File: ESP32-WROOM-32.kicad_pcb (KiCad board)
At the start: 2 copper layers, 80 x 80 mm, 26 parts, among them J1 Conn_01x10_Pin, J2 USB_C_Receptacle_USB2.0_16P, J3 Conn_01x10_Pin, J5 Conn_01x05, Q1 S8050, Q2 S8050, SW1 SW_Push, SW2 SW_Push, U1 ESP32-WROOM-32E, U2 AMS1117-3.3, U3 CH340C

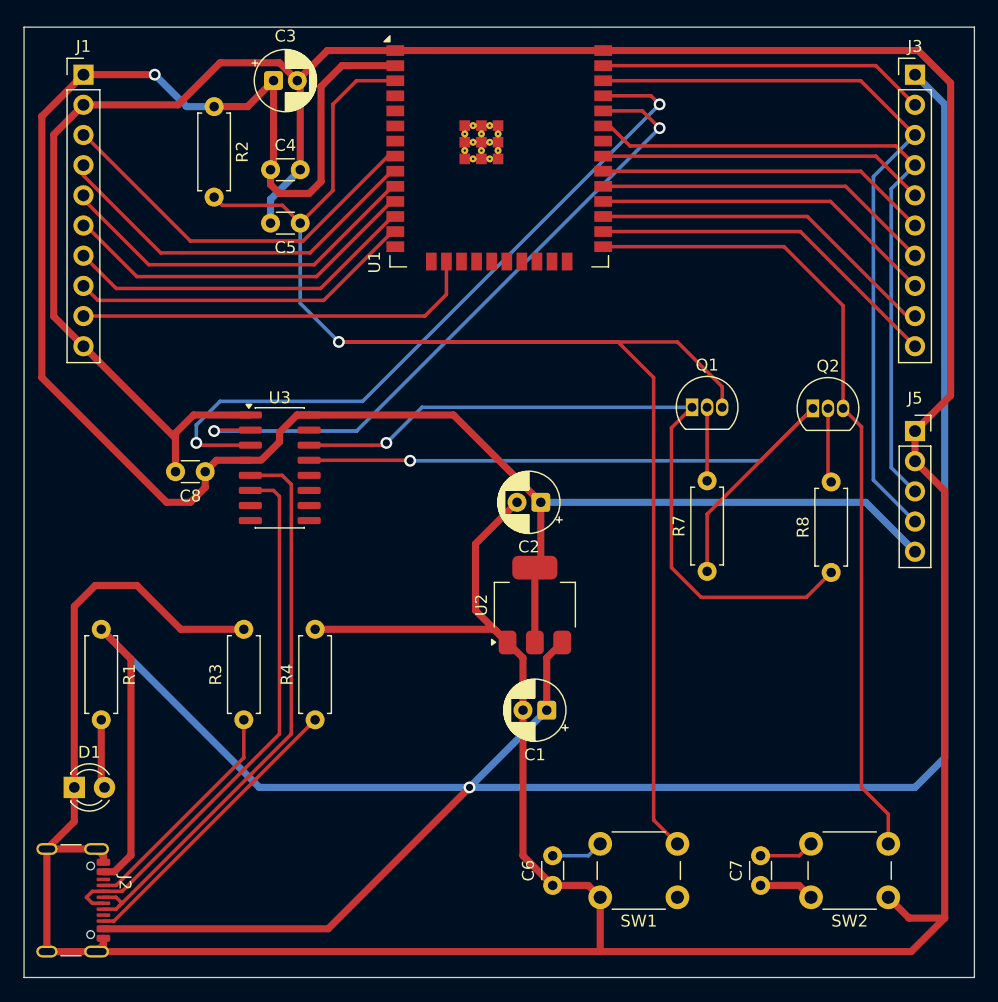
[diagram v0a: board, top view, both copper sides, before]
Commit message: Clean up KiCad project files
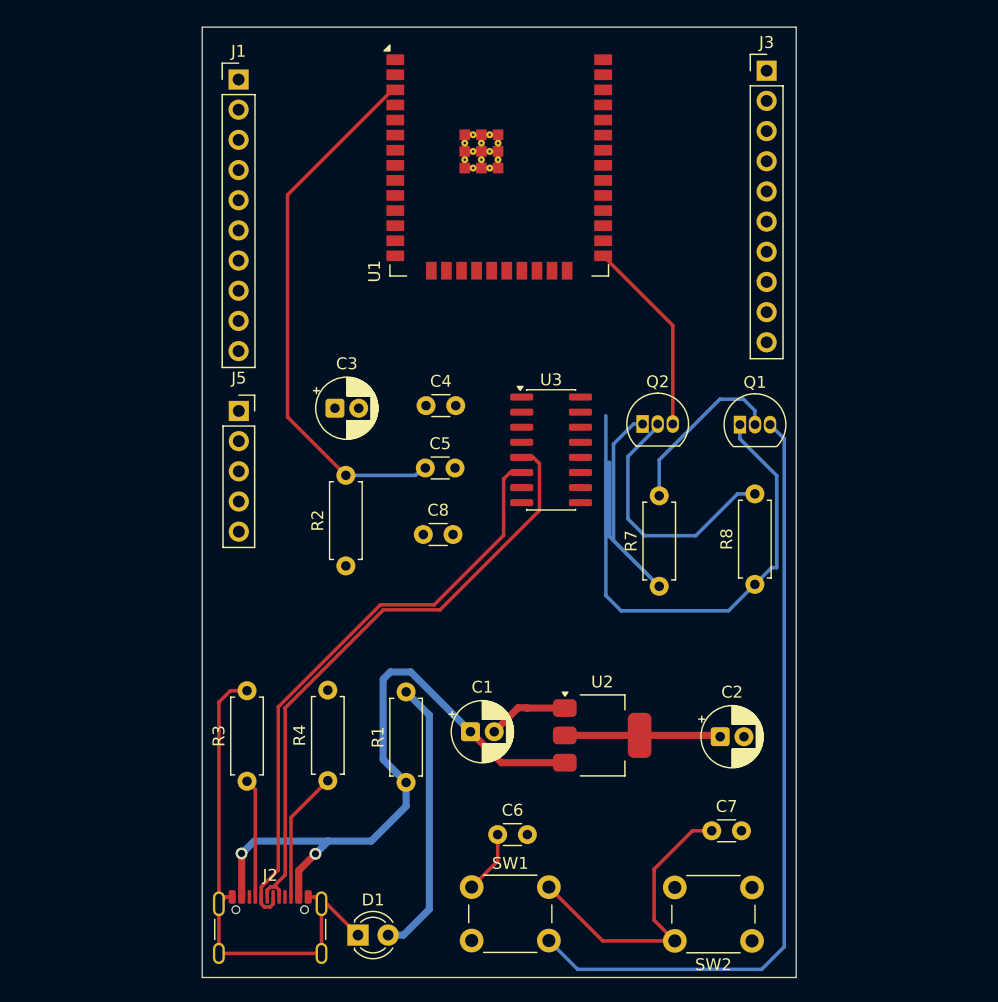
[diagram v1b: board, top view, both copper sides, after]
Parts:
- moved J5 56.9 mm to (128.1, 92.3)
- moved R2 40.2 mm to (137.1, 105.3), turned to 90 degrees
- moved R1 28.7 mm to (142.2, 123.6), turned to 90 degrees
- moved C3 28.1 mm to (136.2, 92.1)
- moved D1 26.9 mm to (138.1, 136.4)
- moved C2 24.8 mm to (168.6, 119.7), turned to 0 degrees
- moved C4 23.8 mm to (143.8, 91.9)
- moved C5 23.1 mm to (143.8, 97.1), turned to 0 degrees
- moved U3 22.9 mm to (154.4, 95.6)
- moved C8 19.1 mm to (143.6, 102.7), turned to 0 degrees
- moved J2 18.0 mm to (130.7, 136.9), turned to 0 degrees
- moved SW1 17.3 mm to (147.7, 132.4), turned to 0 degrees
- moved Q2 14.4 mm to (162.1, 93.4)
- moved J1 13.1 mm to (128.1, 64.4)
- moved J3 12.5 mm to (172.5, 63.7)
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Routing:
- net GND: track 411.6 -> 81.1 mm
- net +3V3: track 171.7 -> 13.1 mm, vias 1 -> 0
- net +5V: track 210.2 -> 55.1 mm, vias 1 -> 2
- net /IO22: track 63.6 -> 0.00 mm
- net /TXD0: track 61.4 -> 0.00 mm, vias 2 -> 0
- net /IO0: track 73.8 -> 16.6 mm
- net /IO21: track 56.7 -> 0.00 mm
- net /RXD0: track 56.5 -> 0.00 mm, vias 2 -> 0
- net /IO13: track 34.1 -> 0.00 mm
- net /EN: track 144.5 -> 111.4 mm, vias 1 -> 0
- net /IO32: track 32.9 -> 0.00 mm
- net /DTR: track 61.6 -> 28.9 mm, vias 1 -> 0
- net /IO33: track 32.7 -> 0.00 mm
- net /IO25: track 31.6 -> 0.00 mm
- net /IO26: track 30.7 -> 0.00 mm
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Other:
- board size 80 x 80 mm -> 50 x 80 mm

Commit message: Replace old ESP32 design with updated ESP32-WROOM-32 project
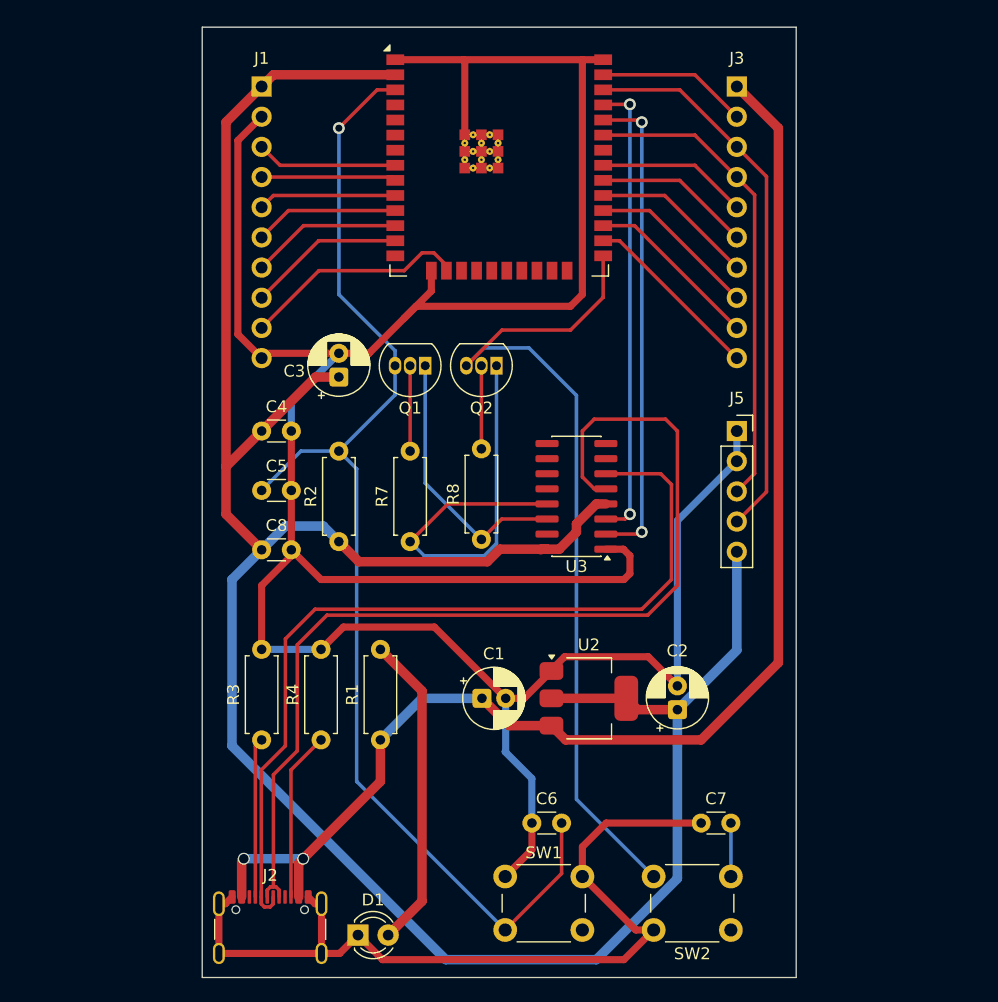
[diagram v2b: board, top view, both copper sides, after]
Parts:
- J1, J3: moved to B.Cu
- moved J5 42.0 mm to (170.0, 94.0)
- moved Q1 27.0 mm to (143.8, 88.5), turned to 180 degrees
- moved R8 23.3 mm to (148.5, 103.1)
- moved R7 21.3 mm to (142.5, 103.3)
- moved C4 14.0 mm to (130.0, 94.0)
- moved C5 13.9 mm to (130.0, 99.0)
- moved C8 13.7 mm to (130.0, 104.0)
- moved Q2 13.2 mm to (149.8, 88.5), turned to 180 degrees
- moved U3 4.46 mm to (156.5, 99.5), turned to 180 degrees
- moved C2 4.26 mm to (165.0, 117.5), turned to 90 degrees
- moved R1 4.18 mm to (140.0, 120.0)
- moved R3 3.69 mm to (130.0, 120.0)
- moved R4 3.48 mm to (135.0, 120.0)
- moved U2 3.32 mm to (157.5, 116.5)
- moved C6 3.04 mm to (152.8, 127.0)
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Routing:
- net GND: track 81.1 -> 313.5 mm
- net +3V3: track 13.1 -> 205.7 mm
- net /IO0: track 16.6 -> 76.6 mm
- net +5V: track 55.1 -> 113.4 mm
- net /IO22: track 0.00 -> 46.8 mm
- net /RXD0: track 0.00 -> 40.9 mm, vias 0 -> 2
- net /IO21: track 0.00 -> 40.4 mm
- net /TXD0: track 0.00 -> 39.0 mm, vias 0 -> 2
- net /USB_DP: track 51.8 -> 85.7 mm
- net /USB_DN: track 50.4 -> 73.4 mm
- net /RTS: track 44.9 -> 22.8 mm
- net /IO13: track 0.00 -> 19.1 mm
- net /IO4: track 0.00 -> 15.3 mm
- net /IO16: track 0.00 -> 14.8 mm
- net Net-(Q2-B): track 21.8 -> 7.00 mm
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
